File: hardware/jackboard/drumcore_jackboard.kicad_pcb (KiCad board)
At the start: 2 copper layers, 210 x 70 mm, 11 parts, among them J1 PAD1_TRS_6.35MM, J2 PAD2_TRS_6.35MM, J3 PAD3_TRS_6.35MM, J4 PAD4_TRS_6.35MM, J5 PAD5_TRS_6.35MM, J6 PAD6_TRS_6.35MM, J7 PAD7_TRS_6.35MM, J8 PAD8_TRS_6.35MM, J9 LINK_TO_MAINBOARD, U1 HC4067_CHANNELS, U2 HC4067_CTRL

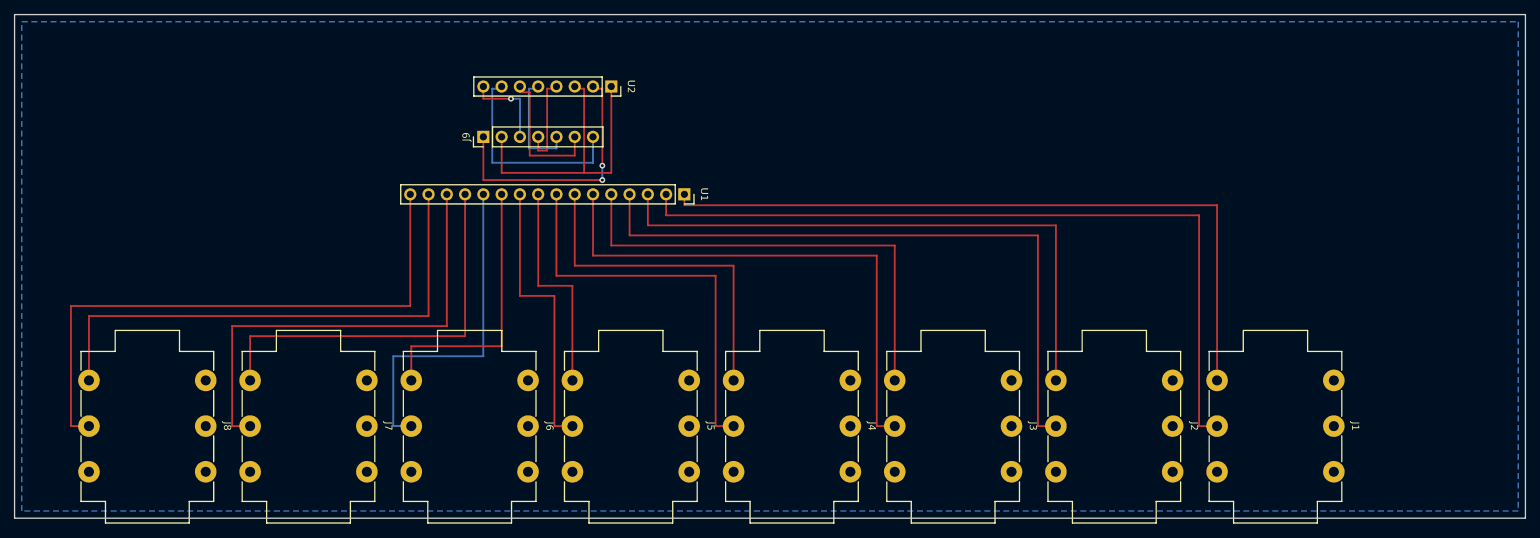
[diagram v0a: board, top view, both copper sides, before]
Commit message: Jackboard: pinos T/R corrigidos + rede de protecao por canal; teste do sensor hall
Hardware (hardware/jackboard):
- Esquematico: jacks usavam TN/RN (contato normal/switched) como sinal por
  engano - corrigido pra usar T/R de verdade (Tip=par, Ring=impar), com
  TN/RN/S/SN todos em GND.
- Adicionada rede de protecao por canal (16x): resistor serie 100R + resistor
  paralelo 100k + diodo BAT85, mesma topologia do esquema de referencia da
  HelloDrum-arduino-Library pro MUX (docs/circuit.md).
- PCB: jacks recriados com a netlist corrigida (sync limpo, sem conflito de
  net reatribuido em pad ja roteado) e realinhados no passo fisico de
  22.5mm; os 48 componentes de protecao posicionados no espaco livre entre
  as duas colunas de pads de cada jack; cluster do mux (U1/U2) e do header
  de link (J9) recentralizado sobre a fileira de jacks.

Firmware:
- main.cpp: teste direto do sensor hall (SS49E) do controlador de HH agora
  le so' o GPIO17 (Pad 1 como PAD_SINGLE) - antes lia GPIO17+18 como
  dual-zone, com o segundo canal flutuando sem sensor conectado.
- Novo ambiente isolado [env:test_hall] (src/test_hall.cpp) - mostra a
  leitura bruta do ADC (0-4095) do GPIO17 na tela TFT + Serial, sem
  MUX/encoders/USB-MIDI/BLE/EEPROM, pra validar o sensor isoladamente.

Checkpoint antes de reduzir de 2 pra 1 encoder rotativo na UI - versiona o
estado atual pra poder reverter se a mudanca nao ficar boa.

Co-Authored-By: Claude Sonnet 5 <noreply@anthropic.com>
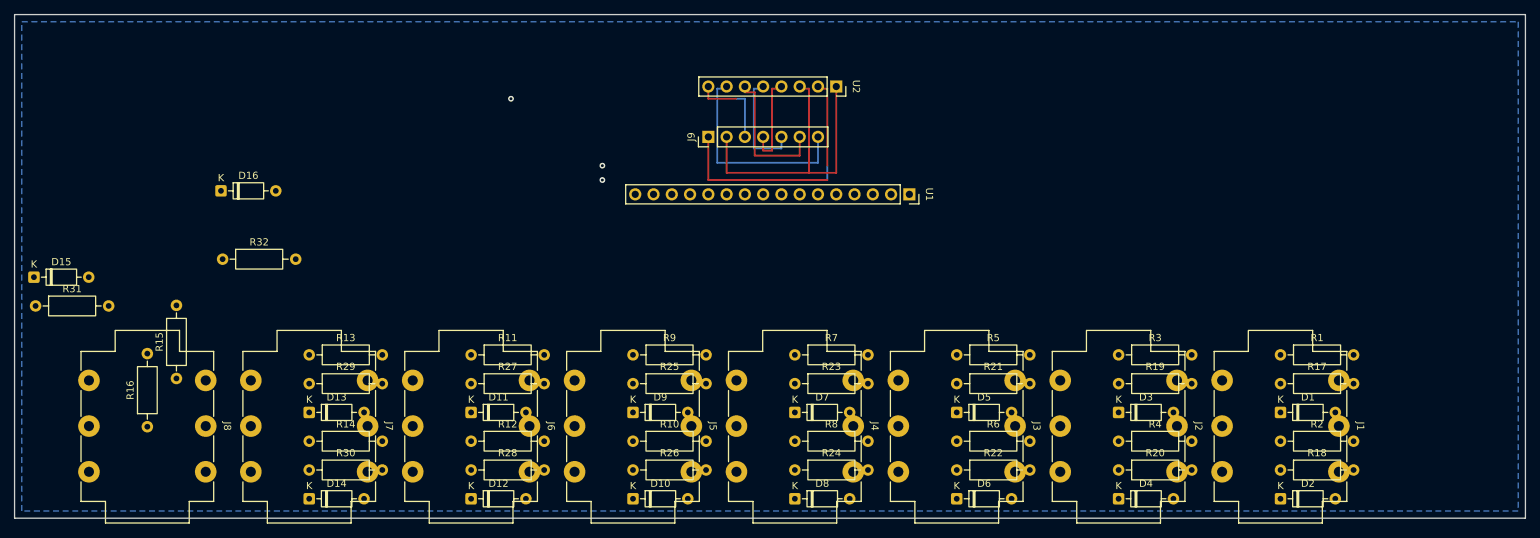
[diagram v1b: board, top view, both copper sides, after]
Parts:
- added D1: BAT85, Diode_THT:D_DO-35_SOD27_P7.62mm_Horizontal, F.Cu at (211.0, 130.3)
- added D10: BAT85, Diode_THT:D_DO-35_SOD27_P7.62mm_Horizontal, F.Cu at (121.0, 142.3)
- added D11: BAT85, Diode_THT:D_DO-35_SOD27_P7.62mm_Horizontal, F.Cu at (98.5, 130.3)
- added D12: BAT85, Diode_THT:D_DO-35_SOD27_P7.62mm_Horizontal, F.Cu at (98.5, 142.3)
- added D13: BAT85, Diode_THT:D_DO-35_SOD27_P7.62mm_Horizontal, F.Cu at (76.0, 130.3)
- added D14: BAT85, Diode_THT:D_DO-35_SOD27_P7.62mm_Horizontal, F.Cu at (76.0, 142.3)
- added D15: BAT85, Diode_THT:D_DO-35_SOD27_P7.62mm_Horizontal, F.Cu at (37.7, 111.5)
- added D16: BAT85, Diode_THT:D_DO-35_SOD27_P7.62mm_Horizontal, F.Cu at (63.7, 99.5)
- added D2: BAT85, Diode_THT:D_DO-35_SOD27_P7.62mm_Horizontal, F.Cu at (211.0, 142.3)
- added D3: BAT85, Diode_THT:D_DO-35_SOD27_P7.62mm_Horizontal, F.Cu at (188.5, 130.3)
- added D4: BAT85, Diode_THT:D_DO-35_SOD27_P7.62mm_Horizontal, F.Cu at (188.5, 142.3)
- added D5: BAT85, Diode_THT:D_DO-35_SOD27_P7.62mm_Horizontal, F.Cu at (166.0, 130.3)
- added D6: BAT85, Diode_THT:D_DO-35_SOD27_P7.62mm_Horizontal, F.Cu at (166.0, 142.3)
- added D7: BAT85, Diode_THT:D_DO-35_SOD27_P7.62mm_Horizontal, F.Cu at (143.5, 130.3)
- added D8: BAT85, Diode_THT:D_DO-35_SOD27_P7.62mm_Horizontal, F.Cu at (143.5, 142.3)
- added D9: BAT85, Diode_THT:D_DO-35_SOD27_P7.62mm_Horizontal, F.Cu at (121.0, 130.3)
- added R1: 100R, Resistor_THT:R_Axial_DIN0207_L6.3mm_D2.5mm_P10.16mm_Horizontal, F.Cu at (211.0, 122.3)
- added R10: 100R, Resistor_THT:R_Axial_DIN0207_L6.3mm_D2.5mm_P10.16mm_Horizontal, F.Cu at (121.0, 134.3)
- added R11: 100R, Resistor_THT:R_Axial_DIN0207_L6.3mm_D2.5mm_P10.16mm_Horizontal, F.Cu at (98.5, 122.3)
- added R12: 100R, Resistor_THT:R_Axial_DIN0207_L6.3mm_D2.5mm_P10.16mm_Horizontal, F.Cu at (98.5, 134.3)
- added R13: 100R, Resistor_THT:R_Axial_DIN0207_L6.3mm_D2.5mm_P10.16mm_Horizontal, F.Cu at (76.0, 122.3)
- added R14: 100R, Resistor_THT:R_Axial_DIN0207_L6.3mm_D2.5mm_P10.16mm_Horizontal, F.Cu at (76.0, 134.3)
- added R15: 100R, Resistor_THT:R_Axial_DIN0207_L6.3mm_D2.5mm_P10.16mm_Horizontal, F.Cu at (57.5, 125.6)
- added R16: 100R, Resistor_THT:R_Axial_DIN0207_L6.3mm_D2.5mm_P10.16mm_Horizontal, F.Cu at (53.5, 132.3)
- added R17: 100K, Resistor_THT:R_Axial_DIN0207_L6.3mm_D2.5mm_P10.16mm_Horizontal, F.Cu at (211.0, 126.3)
- added R18: 100K, Resistor_THT:R_Axial_DIN0207_L6.3mm_D2.5mm_P10.16mm_Horizontal, F.Cu at (211.0, 138.3)
- added R19: 100K, Resistor_THT:R_Axial_DIN0207_L6.3mm_D2.5mm_P10.16mm_Horizontal, F.Cu at (188.5, 126.3)
- added R2: 100R, Resistor_THT:R_Axial_DIN0207_L6.3mm_D2.5mm_P10.16mm_Horizontal, F.Cu at (211.0, 134.3)
- added R20: 100K, Resistor_THT:R_Axial_DIN0207_L6.3mm_D2.5mm_P10.16mm_Horizontal, F.Cu at (188.5, 138.3)
- added R21: 100K, Resistor_THT:R_Axial_DIN0207_L6.3mm_D2.5mm_P10.16mm_Horizontal, F.Cu at (166.0, 126.3)
- added R22: 100K, Resistor_THT:R_Axial_DIN0207_L6.3mm_D2.5mm_P10.16mm_Horizontal, F.Cu at (166.0, 138.3)
- added R23: 100K, Resistor_THT:R_Axial_DIN0207_L6.3mm_D2.5mm_P10.16mm_Horizontal, F.Cu at (143.5, 126.3)
- added R24: 100K, Resistor_THT:R_Axial_DIN0207_L6.3mm_D2.5mm_P10.16mm_Horizontal, F.Cu at (143.5, 138.3)
- added R25: 100K, Resistor_THT:R_Axial_DIN0207_L6.3mm_D2.5mm_P10.16mm_Horizontal, F.Cu at (121.0, 126.3)
- added R26: 100K, Resistor_THT:R_Axial_DIN0207_L6.3mm_D2.5mm_P10.16mm_Horizontal, F.Cu at (121.0, 138.3)
- added R27: 100K, Resistor_THT:R_Axial_DIN0207_L6.3mm_D2.5mm_P10.16mm_Horizontal, F.Cu at (98.5, 126.3)
- added R28: 100K, Resistor_THT:R_Axial_DIN0207_L6.3mm_D2.5mm_P10.16mm_Horizontal, F.Cu at (98.5, 138.3)
- added R29: 100K, Resistor_THT:R_Axial_DIN0207_L6.3mm_D2.5mm_P10.16mm_Horizontal, F.Cu at (76.0, 126.3)
- added R3: 100R, Resistor_THT:R_Axial_DIN0207_L6.3mm_D2.5mm_P10.16mm_Horizontal, F.Cu at (188.5, 122.3)
- added R30: 100K, Resistor_THT:R_Axial_DIN0207_L6.3mm_D2.5mm_P10.16mm_Horizontal, F.Cu at (76.0, 138.3)
- added R31: 100K, Resistor_THT:R_Axial_DIN0207_L6.3mm_D2.5mm_P10.16mm_Horizontal, F.Cu at (37.9, 115.5)
- added R32: 100K, Resistor_THT:R_Axial_DIN0207_L6.3mm_D2.5mm_P10.16mm_Horizontal, F.Cu at (63.9, 109.0)
- added R4: 100R, Resistor_THT:R_Axial_DIN0207_L6.3mm_D2.5mm_P10.16mm_Horizontal, F.Cu at (188.5, 134.3)
- added R5: 100R, Resistor_THT:R_Axial_DIN0207_L6.3mm_D2.5mm_P10.16mm_Horizontal, F.Cu at (166.0, 122.3)
- added R6: 100R, Resistor_THT:R_Axial_DIN0207_L6.3mm_D2.5mm_P10.16mm_Horizontal, F.Cu at (166.0, 134.3)
- added R7: 100R, Resistor_THT:R_Axial_DIN0207_L6.3mm_D2.5mm_P10.16mm_Horizontal, F.Cu at (143.5, 122.3)
- added R8: 100R, Resistor_THT:R_Axial_DIN0207_L6.3mm_D2.5mm_P10.16mm_Horizontal, F.Cu at (143.5, 134.3)
- added R9: 100R, Resistor_THT:R_Axial_DIN0207_L6.3mm_D2.5mm_P10.16mm_Horizontal, F.Cu at (121.0, 122.3)
- moved J9 31.3 mm to (131.4, 92.0)
- moved U1 31.3 mm to (159.4, 100.0)
- moved U2 31.3 mm to (149.2, 85.0)
- moved J1 0.70 mm to (219.1, 125.8)
- moved J2 0.60 mm to (196.6, 125.8)
- moved J3 0.50 mm to (174.1, 125.8)
- moved J4 0.40 mm to (151.6, 125.8)
- moved J5 0.30 mm to (129.1, 125.8)
- moved J6 0.20 mm to (106.6, 125.8)
- moved J7 0.10 mm to (84.1, 125.8)
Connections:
- J1 pad R: /GND -> /MUX_C1_RAW
- J1 pad RN: /MUX_C1 -> /GND
- J1 pad T: /GND -> /MUX_C0_RAW
- J1 pad TN: /MUX_C0 -> /GND
- J2 pad R: /GND -> /MUX_C3_RAW
- J2 pad RN: /MUX_C3 -> /GND
- J2 pad T: /GND -> /MUX_C2_RAW
- J2 pad TN: /MUX_C2 -> /GND
- J3 pad R: /GND -> /MUX_C5_RAW
- J3 pad RN: /MUX_C5 -> /GND
- J3 pad T: /GND -> /MUX_C4_RAW
- J3 pad TN: /MUX_C4 -> /GND
- J4 pad R: /GND -> /MUX_C7_RAW
- J4 pad RN: /MUX_C7 -> /GND
- J4 pad T: /GND -> /MUX_C6_RAW
- J4 pad TN: /MUX_C6 -> /GND
- J5 pad R: /GND -> /MUX_C9_RAW
- J5 pad RN: /MUX_C9 -> /GND
- J5 pad T: /GND -> /MUX_C8_RAW
- J5 pad TN: /MUX_C8 -> /GND
- J6 pad R: /GND -> /MUX_C11_RAW
- J6 pad RN: /MUX_C11 -> /GND
- J6 pad T: /GND -> /MUX_C10_RAW
- J6 pad TN: /MUX_C10 -> /GND
- J7 pad R: /GND -> /MUX_C13_RAW
- J7 pad RN: /MUX_C13 -> /GND
- J7 pad T: /GND -> /MUX_C12_RAW
- J7 pad TN: /MUX_C12 -> /GND
- J8 pad R: /GND -> /MUX_C15_RAW
- J8 pad RN: /MUX_C15 -> /GND
- J8 pad T: /GND -> /MUX_C14_RAW
- J8 pad TN: /MUX_C14 -> /GND
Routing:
- net /MUX_C1: track 108.8 -> 0.00 mm
- net /MUX_C0: track 99.9 -> 0.00 mm
- net /MUX_C3: track 91.5 -> 0.00 mm
- net /MUX_C2: track 82.6 -> 0.00 mm
- net /MUX_C15: track 81.9 -> 0.00 mm
- net /MUX_C5: track 74.2 -> 0.00 mm
- net /MUX_C14: track 73.1 -> 0.00 mm
- net /MUX_C4: track 65.3 -> 0.00 mm
- net /MUX_C13: track 64.6 -> 0.00 mm
- net /MUX_C7: track 56.8 -> 0.00 mm
- net /MUX_C12: track 55.7 -> 0.00 mm
- net /MUX_C6: track 47.9 -> 0.00 mm
- net /MUX_C11: track 47.2 -> 0.00 mm
- net /MUX_C9: track 39.5 -> 0.00 mm
- net /MUX_C10: track 38.4 -> 0.00 mm
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
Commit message: Jackboard: roteamento completo, logo, GND ajustado; docs e site atualizados
- Jackboard: roteamento completo (0 curtos/desconectados no DRC), U1/U2
  recentralizados, logo "DRUMCORE" na serigrafia (F.SilkS), pad de teste
  +3V3 no estilo dos resistores, placa redimensionada (rosca do jack pra
  fora) com malha de GND reajustada. Gerbers regenerados em
  hardware/jackboard/fab/.
- mainboard aposentada (fiação simplificada dispensa PCB dedicada) e
  simulador de hardware do app desktop removido (2 encoders -> 1).
- Documentação revisada e atualizada: README (mux/tela/estrutura
  desatualizados), design/SPEC.md (referência a "DIN" inexistente),
  design/LOGOS.md (direção de logo escolhida), docs/02-hardware.md
  (cross-referência à jackboard), CHANGELOG (nova entrada).
- Publicado site/ estático (GitHub Pages) com visão geral, hardware e
  instruções de flash do firmware.

Co-Authored-By: Claude Sonnet 5 <noreply@anthropic.com>
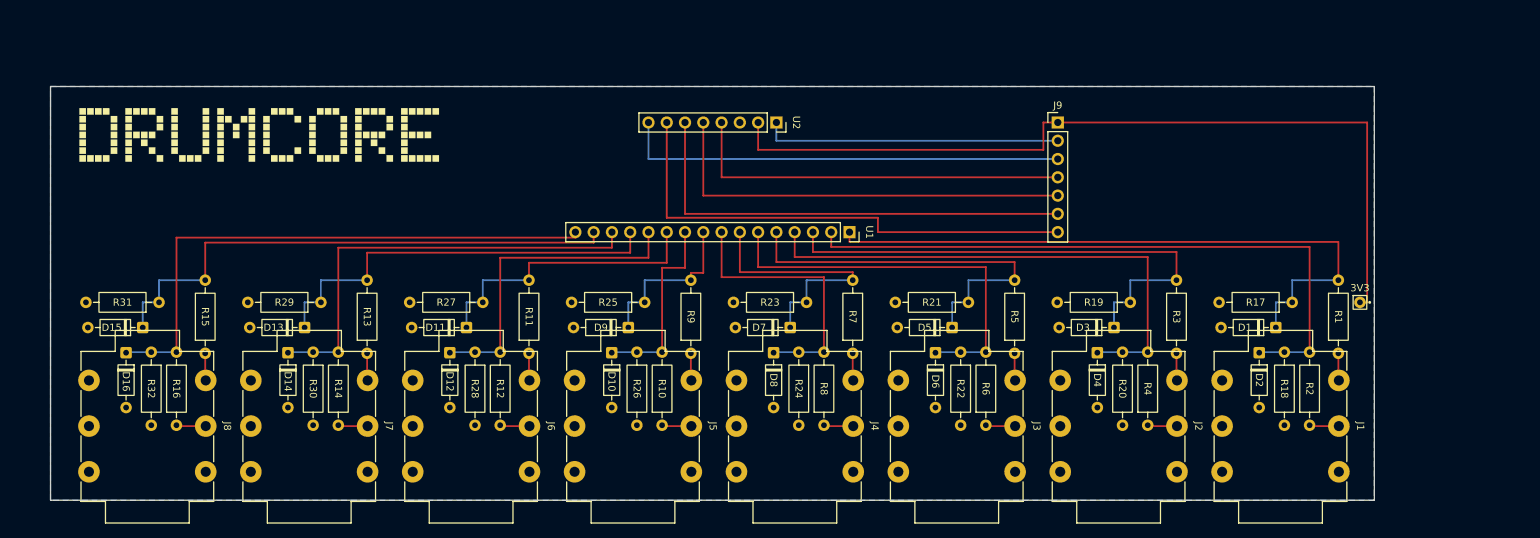
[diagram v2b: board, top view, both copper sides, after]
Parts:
- added 3V3: TestPoint_3V3, drumcore_jackboard:TestPoint_3V3, F.Cu at (222.0, 115.0)
- moved J9 48.6 mm to (180.0, 90.0), turned to 0 degrees
- moved D16 26.1 mm to (50.5, 122.0), turned to -90 degrees
- moved D2 20.5 mm to (208.0, 122.0), turned to -90 degrees
- moved D4 20.5 mm to (185.5, 122.0), turned to -90 degrees
- moved D6 20.5 mm to (163.0, 122.0), turned to -90 degrees
- moved D8 20.5 mm to (140.5, 122.0), turned to -90 degrees
- moved D10 20.5 mm to (118.0, 122.0), turned to -90 degrees
- moved D12 20.5 mm to (95.5, 122.0), turned to -90 degrees
- moved D14 20.5 mm to (73.0, 122.0), turned to -90 degrees
- moved R31 17.2 mm to (55.1, 115.0), turned to 180 degrees
- moved D15 16.7 mm to (52.8, 118.5), turned to 180 degrees
- moved R18 16.4 mm to (211.5, 121.9), turned to -90 degrees
- moved R20 16.4 mm to (189.0, 121.9), turned to -90 degrees
- moved R22 16.4 mm to (166.5, 121.9), turned to -90 degrees
- moved R24 16.4 mm to (144.0, 121.9), turned to -90 degrees
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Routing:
- net /MUX_C1: track 0.00 -> 90.3 mm
- net /MUX_C0: track 0.00 -> 89.9 mm
- net /+3V3: track 36.8 -> 118.2 mm, vias 2 -> 0
- net /MUX_C15: track 0.00 -> 79.2 mm
- net /MUX_C14: track 0.00 -> 75.9 mm
- net /MUX_C3: track 0.00 -> 72.8 mm
- net /MUX_C2: track 0.00 -> 72.5 mm
- net /MUX_C13: track 0.00 -> 61.8 mm
- net /MUX_C12: track 0.00 -> 58.5 mm
- net /MUX_C5: track 0.00 -> 55.4 mm
- net /MUX_C4: track 0.00 -> 55.1 mm
- net /MUX_SIG: track 12.1 -> 62.0 mm, vias 1 -> 0
- net /MUX_S2: track 19.8 -> 64.5 mm
- net /MUX_C11: track 0.00 -> 44.4 mm
- net /MUX_S1: track 15.3 -> 59.4 mm
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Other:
- board size 210 x 70 mm -> 184 x 57.5 mm
